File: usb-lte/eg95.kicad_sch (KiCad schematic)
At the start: 25 parts, among them J2 Conn_Coaxial, J3 Conn_Coaxial, J4 Conn_Coaxial, U2 EG95

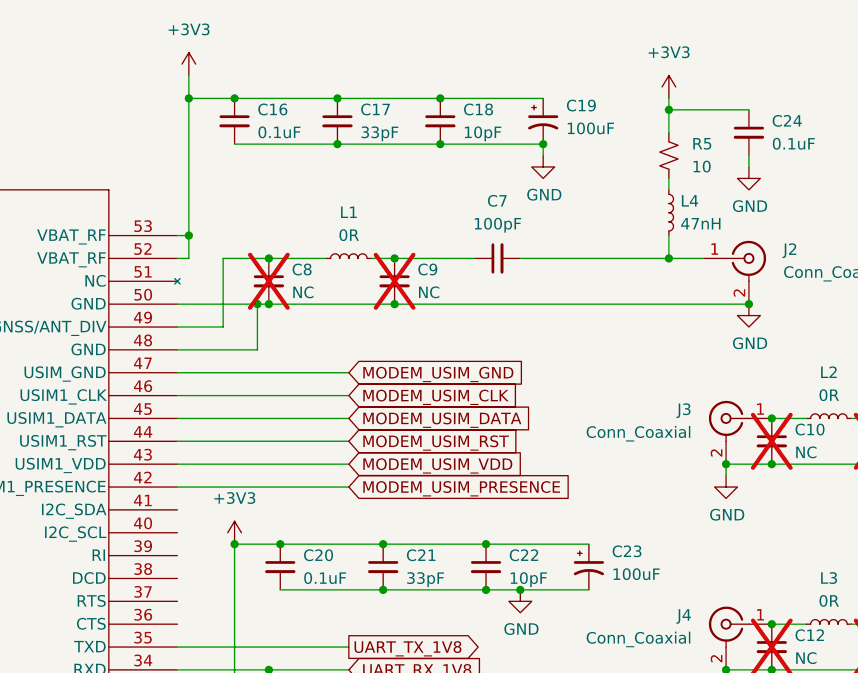
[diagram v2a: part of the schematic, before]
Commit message: Use SMPS and 3.8V for module
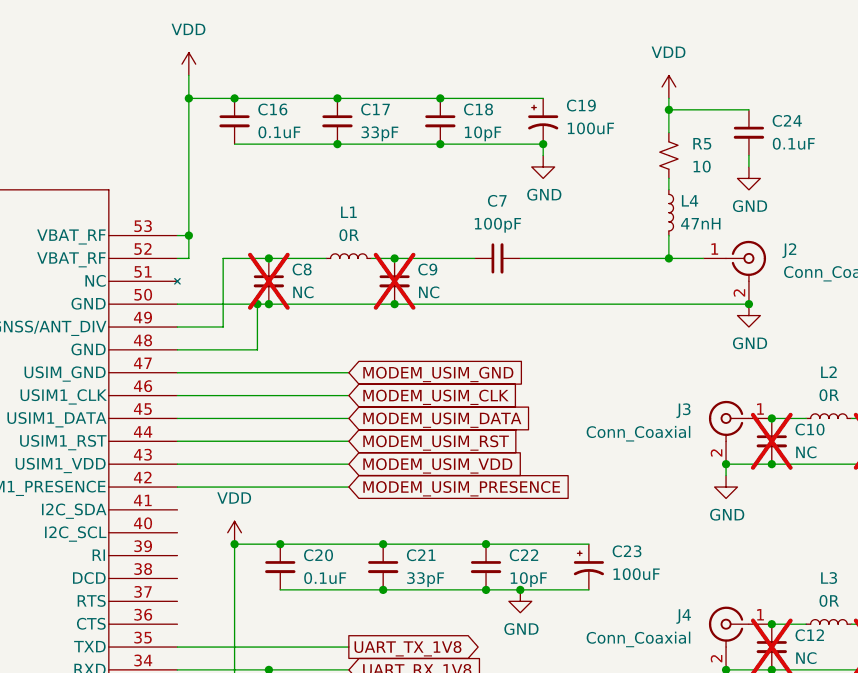
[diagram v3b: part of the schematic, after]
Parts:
- R5: footprint Resistor_SMD:R_0402_1005Metric_Pad0.72x0.64mm_HandSolder -> Resistor_SMD:R_0402_1005Metric
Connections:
- net +3V3 renamed VDD
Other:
- company: (none) -> Zokhoi
- title: (none) -> Framework LTE Expansion Card
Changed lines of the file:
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@@
 	(generator_version "8.0")
 	(paper "A4")
+	(title_block
+		(title "Framework LTE Expansion Card")
+		(date "2025-03-26")
+		(rev "0")
+		(company "Zokhoi")
+	)
 	(junction
 		(at 171.45 66.04)
@@
 	)
 	(junction
+		(at 116.84 74.93)
+		(diameter 0)
+		(color 0 0 0 0)
+	)
+	(junction
 		(at 195.58 116.84)
 		(diameter 0)
@@
 	)
 	(junction
-		(at 116.84 74.93)
-		(diameter 0)
-		(color 0 0 0 0)
-	)
-	(junction
 		(at 121.92 74.93)
 		(diameter 0)
@@
 	)
 	(symbol
-		(lib_id "power:+3V3")
-		(at 165.1 25.4 0)
+		(lib_id "Device:C_Small")
+		(at 120.65 45.72 0)
 		(unit 1)
 		(exclude_from_sim no)
 		(in_bom yes)
 		(on_board yes)
-		(dnp no)
+		(dnp yes)
 		(fields_autoplaced yes)
-		(property "Reference" "#PWR14"
-			(at 165.1 29.21 0)
+		(property "Reference" "C8"
+			(at 123.19 44.4562 0)
 			(effects
 				(font
 					(size 1.27 1.27)
 				)
-				(hide yes)
+				(justify left)
 			)
 		)
-		(property "Value" "+3V3"
-			(at 165.1 20.32 0)
+		(property "Value" "NC"
+			(at 123.19 46.9962 0)
 			(effects
 				(font
 					(size 1.27 1.27)
 				)
+				(justify left)
 			)
 		)
-		(property "Footprint" ""
-			(at 165.1 25.4 0)
+		(property "Footprint" "Capacitor_SMD:C_0402_1005Metric"
+			(at 120.65 45.72 0)
 			(effects
 				(font
@@
 			)
 		)
-		(property "Datasheet" ""
-			(at 165.1 25.4 0)
+		(property "Datasheet" "~"
+			(at 120.65 45.72 0)
 			(effects
 				(font
@@
 			)
 		)
-		(property "Description" "Power symbol creates a global label with name \"+3V3\""
-			(at 165.1 25.4 0)
+		(property "Description" "Unpolarized capacitor, small symbol"
+			(at 120.65 45.72 0)
 			(effects
 				(font
@@
 		(pin "1"
 		)
+		(pin "2"
+		)
 		(instances
-			(project "usb-lte"
+			(project ""
 				(path "/81dea973-9ff3-499f-8a46-acefd4a76150/6c47dcf9-5816-4ed5-88a6-9e570374b167"
-					(reference "#PWR14")
+					(reference "C8")
 					(unit 1)
 				)
@@
 	)
 	(symbol
-		(lib_id "Device:C_Small")
-		(at 120.65 45.72 0)
+		(lib_id "power:VDD")
+		(at 116.84 74.93 0)
 		(unit 1)
 		(exclude_from_sim no)
 		(in_bom yes)
 		(on_board yes)
-		(dnp yes)
+		(dnp no)
 		(fields_autoplaced yes)
-		(property "Reference" "C8"
-			(at 123.19 44.4562 0)
+		(property "Reference" "#PWR14"
+			(at 116.84 78.74 0)
 			(effects
 				(font
 					(size 1.27 1.27)
 				)
-				(justify left)
+				(hide yes)
 			)
 		)
-		(property "Value" "NC"
-			(at 123.19 46.9962 0)
+		(property "Value" "VDD"
+			(at 116.84 69.85 0)
 			(effects
 				(font
 					(size 1.27 1.27)
 				)
-				(justify left)
 			)
 		)
-		(property "Footprint" "Capacitor_SMD:C_0402_1005Metric"
-			(at 120.65 45.72 0)
+		(property "Footprint" ""
+			(at 116.84 74.93 0)
 			(effects
 				(font
@@
 			)
 		)
-		(property "Datasheet" "~"
-			(at 120.65 45.72 0)
+		(property "Datasheet" ""
+			(at 116.84 74.93 0)
 			(effects
 				(font
@@
 			)
 		)
-		(property "Description" "Unpolarized capacitor, small symbol"
-			(at 120.65 45.72 0)
+		(property "Description" "Power symbol creates a global label with name \"VDD\""
+			(at 116.84 74.93 0)
 			(effects
 				(font
@@
 		(pin "1"
 		)
-		(pin "2"
-		)
 		(instances
-			(project ""
+			(project "usb-lte"
 				(path "/81dea973-9ff3-499f-8a46-acefd4a76150/6c47dcf9-5816-4ed5-88a6-9e570374b167"
-					(reference "C8")
+					(reference "#PWR14")
 					(unit 1)
 				)
@@
 	)
 	(symbol
+		(lib_id "power:VDD")
+		(at 165.1 25.4 0)
+		(unit 1)
+		(exclude_from_sim no)
+		(in_bom yes)
+		(on_board yes)
+		(dnp no)
+		(fields_autoplaced yes)
+		(property "Reference" "#PWR8"
+			(at 165.1 29.21 0)
+			(effects
+				(font
+					(size 1.27 1.27)
+				)
+				(hide yes)
+			)
+		)
+		(property "Value" "VDD"
+			(at 165.1 20.32 0)
+			(effects
+				(font
+					(size 1.27 1.27)
+				)
+			)
+		)
+		(property "Footprint" ""
+			(at 165.1 25.4 0)
+			(effects
+				(font
+					(size 1.27 1.27)
+				)
+				(hide yes)
+			)
+		)
+		(property "Datasheet" ""
+			(at 165.1 25.4 0)
+			(effects
+				(font
+					(size 1.27 1.27)
+				)
+				(hide yes)
+			)
+		)
+		(property "Description" "Power symbol creates a global label with name \"VDD\""
+			(at 165.1 25.4 0)
+			(effects
+				(font
+					(size 1.27 1.27)
+				)
+				(hide yes)
+			)
+		)
+		(pin "1"
+		)
+		(instances
+			(project "usb-lte"
+				(path "/81dea973-9ff3-499f-8a46-acefd4a76150/6c47dcf9-5816-4ed5-88a6-9e570374b167"
+					(reference "#PWR8")
+					(unit 1)
+				)
+			)
+		)
+	)
+	(symbol
 		(lib_id "Device:L_Small")
 		(at 165.1 38.1 0)
@@
 	)
 	(symbol
-		(lib_id "power:+3V3")
-		(at 116.84 74.93 0)
-		(unit 1)
-		(exclude_from_sim no)
-		(in_bom yes)
-		(on_board yes)
-		(dnp no)
-		(fields_autoplaced yes)
-		(property "Reference" "#PWR27"
-			(at 116.84 78.74 0)
-			(effects
-				(font
-					(size 1.27 1.27)
-				)
-				(hide yes)
-			)
-		)
-		(property "Value" "+3V3"
-			(at 116.84 69.85 0)
-			(effects
-				(font
-					(size 1.27 1.27)
-				)
-			)
-		)
-		(property "Footprint" ""
-			(at 116.84 74.93 0)
-			(effects
-				(font
-					(size 1.27 1.27)
-				)
-				(hide yes)
-			)
-		)
-		(property "Datasheet" ""
-			(at 116.84 74.93 0)
-			(effects
-				(font
-					(size 1.27 1.27)
-				)
-				(hide yes)
-			)
-		)
-		(property "Description" "Power symbol creates a global label with name \"+3V3\""
-			(at 116.84 74.93 0)
-			(effects
-				(font
-					(size 1.27 1.27)
-				)
-				(hide yes)
-			)
-		)
-		(pin "1"
-		)
-		(instances
-			(project "usb-lte"
-				(path "/81dea973-9ff3-499f-8a46-acefd4a76150/6c47dcf9-5816-4ed5-88a6-9e570374b167"
-					(reference "#PWR27")
-					(unit 1)
-				)
-			)
-		)
-	)
-	(symbol
 		(lib_id "Device:C_Small")
 		(at 128.27 27.94 0)
@@
 	)
 	(symbol
-		(lib_id "power:+3V3")
-		(at 111.76 22.86 0)
-		(unit 1)
-		(exclude_from_sim no)
-		(in_bom yes)
-		(on_board yes)
-		(dnp no)
-		(fields_autoplaced yes)
-		(property "Reference" "#PWR8"
-			(at 111.76 26.67 0)
-			(effects
-				(font
-					(size 1.27 1.27)
-				)
-				(hide yes)
-			)
-		)
-		(property "Value" "+3V3"
-			(at 111.76 17.78 0)
-			(effects
-				(font
-					(size 1.27 1.27)
-				)
-			)
-		)
-		(property "Footprint" ""
-			(at 111.76 22.86 0)
-			(effects
-				(font
-					(size 1.27 1.27)
-				)
-				(hide yes)
-			)
-		)
-		(property "Datasheet" ""
-			(at 111.76 22.86 0)
-			(effects
-				(font
-					(size 1.27 1.27)
-				)
-				(hide yes)
-			)
-		)
-		(property "Description" "Power symbol creates a global label with name \"+3V3\""
-			(at 111.76 22.86 0)
-			(effects
-				(font
-					(size 1.27 1.27)
-				)
-				(hide yes)
-			)
-		)
-		(pin "1"
-		)
-		(instances
-			(project "usb-lte"
-				(path "/81dea973-9ff3-499f-8a46-acefd4a76150/6c47dcf9-5816-4ed5-88a6-9e570374b167"
-					(reference "#PWR8")
-					(unit 1)
-				)
-			)
-		)
-	)
-	(symbol
 		(lib_id "Device:C_Small")
 		(at 116.84 27.94 0)
@@
 			)
 		)
-		(property "Footprint" "Resistor_SMD:R_0402_1005Metric_Pad0.72x0.64mm_HandSolder"
+		(property "Footprint" "Resistor_SMD:R_0402_1005Metric"
 			(at 165.1 31.75 0)
 			(effects
@@
 					(unit 1)
 				)
+			)
+		)
+	)
+	(symbol
+		(lib_id "power:VDD")
+		(at 111.76 22.86 0)
+		(unit 1)
+		(exclude_from_sim no)
+		(in_bom yes)
+		(on_board yes)
+		(dnp no)
+		(fields_autoplaced yes)
+		(property "Reference" "#PWR6"
+			(at 111.76 26.67 0)
+			(effects
+				(font
+					(size 1.27 1.27)
+				)
+				(hide yes)
+			)
+		)
+		(property "Value" "VDD"
+			(at 111.76 17.78 0)
+			(effects
+				(font
+					(size 1.27 1.27)
+				)
+			)
+		)
+		(property "Footprint" ""
+			(at 111.76 22.86 0)
+			(effects
+				(font
+					(size 1.27 1.27)
+				)
+				(hide yes)
+			)
+		)
+		(property "Datasheet" ""
+			(at 111.76 22.86 0)
+			(effects
+				(font
+					(size 1.27 1.27)
+				)
+				(hide yes)
+			)
+		)
+		(property "Description" "Power symbol creates a global label with name \"VDD\""
+			(at 111.76 22.86 0)
+			(effects
+				(font
+					(size 1.27 1.27)
+				)
+				(hide yes)
+			)
+		)
+		(pin "1"
+		)
+		(instances
+			(project "usb-lte"
+				(path "/81dea973-9ff3-499f-8a46-acefd4a76150/6c47dcf9-5816-4ed5-88a6-9e570374b167"
+					(reference "#PWR6")
+					(unit 1)
+				)

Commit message: Add various test points
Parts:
- added TP12, TP13, TP14, TP15: TestPoint, footprints:TestPoint_Pad_1mm, symbol Connector:TestPoint
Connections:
- net MODEM_NETLIGHT: now also TP15.1
- net MODEM_PWRKEY: now also TP12.1
- net MODEM_RESET: now also TP13.1
- net MODEM_STATUS: now also TP14.1

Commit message: Update 3d models
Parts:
- added D3: LED_Dual_AKKA, footprints:LED_Dual_0805_4pin, symbol Device:LED_Dual_AKKA
- added Q3: MBT3904DW1, Package_TO_SOT_SMD:SOT-363_SC-70-6, symbol Transistor_BJT:MBT3904DW1
- added R21, R22, R23, R24, R27: 4.7k, Resistor_SMD:R_0402_1005Metric, symbol Device:R_Small_US
- added R25, R26: 47k, Resistor_SMD:R_0402_1005Metric, symbol Device:R_Small_US
- added SW1: B3U-1000P, Button_Switch_SMD:SW_SPST_B3U-1000P, symbol Switch:SW_Push
- added TP16, TP17: TestPoint, footprints:TestPoint_Pad_1mm, symbol Connector:TestPoint
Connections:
- net GND: now also Q3.1 (E1), Q3.4 (E2), R25.1, R26.1
- net MODEM_NETLIGHT: now also TP14.1, R24.2; no longer TP15.1
- net MODEM_STATUS: now also TP15.1, R23.2; no longer TP14.1
- net VDD: now also D3.1 (A1), D3.4 (A2)
- net VDD_EXT: now also R27.2, TP16.1
- net MODEM_USB_BOOT: now reaches U2.75 (USB_BOOT)
- net MODEM_USB_BOOT: now also SW1.2, TP17.1
- new net: Q3.2 (B1), R23.1, R25.2
- new net: Q3.5 (B2), R24.1, R26.2
- new net: Q3.6 (C1), R21.2
- new net: D3.2 (K1), R22.1
- new net: Q3.3 (C2), R22.2
- new net: R27.1, SW1.1
- new net: D3.3 (K2), R21.1
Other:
- note added: "Cellular Modem"
- note added: "Green"
- note added: "Red"
- note added: "Status lights"
- note added: "USB Boot key"
- title: Framework LTE Expansion Card -> Framework Cellular Expansion Card
- moved on the sheet: TP12, TP13, TP14, TP15

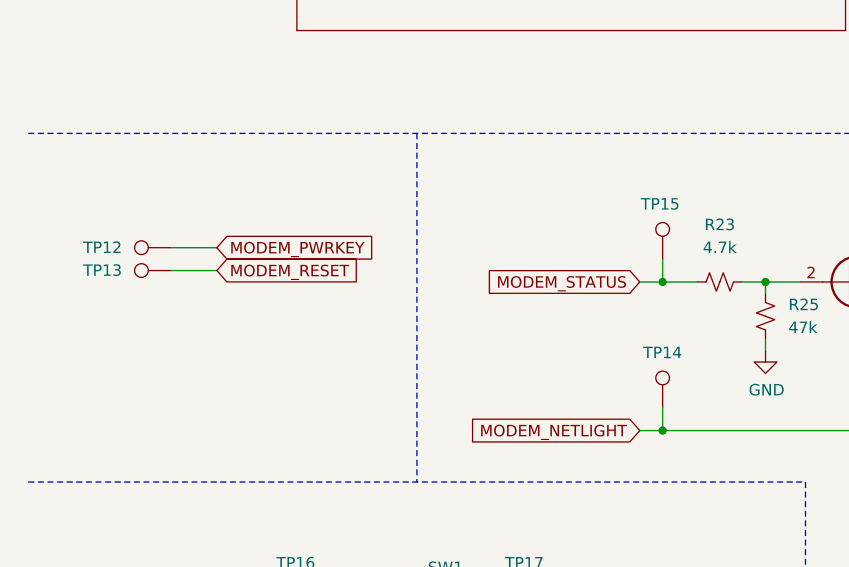
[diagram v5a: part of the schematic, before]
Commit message: Update test points
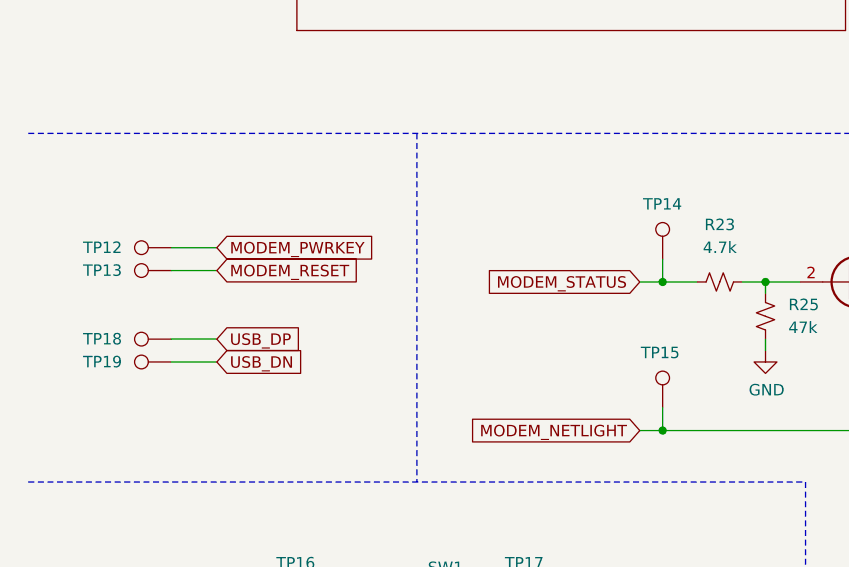
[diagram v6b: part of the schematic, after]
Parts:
- added TP18, TP19: TestPoint, footprints:TestPoint_Pad_1mm, symbol Connector:TestPoint
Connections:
- net MODEM_NETLIGHT: now also TP15.1; no longer TP14.1
- net MODEM_STATUS: now also TP14.1; no longer TP15.1
- net USB_DN: now also TP19.1
- net USB_DP: now also TP18.1

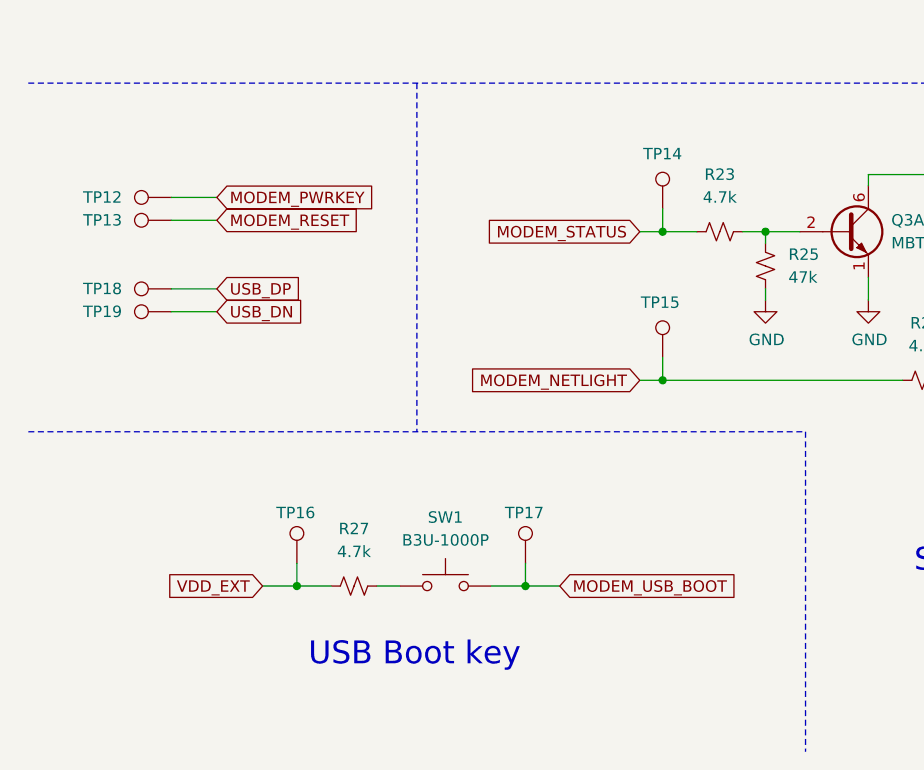
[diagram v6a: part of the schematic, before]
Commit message: Remove USB boot key, add autostart pull down
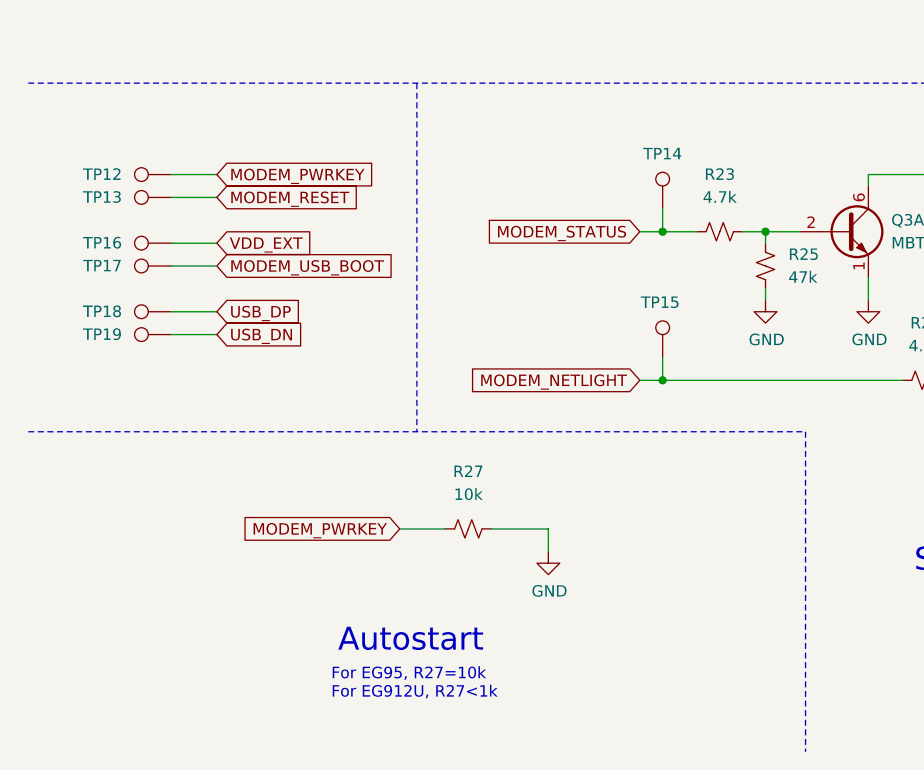
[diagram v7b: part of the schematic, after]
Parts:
- removed SW1: B3U-1000P, Button_Switch_SMD:SW_SPST_B3U-1000P, symbol Switch:SW_Push
- R27: value 4.7k -> 10k
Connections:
- net GND: now also R27.1
- net MODEM_PWRKEY: now also R27.2
- net VDD_EXT: no longer R27.2
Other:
- note added: "Autostart"
- note added: "For EG95, R27=10k For EG912U, R27<1k"
- note removed: "USB Boot key"
- moved on the sheet: TP12, TP13, TP16, TP17, TP18, TP19
